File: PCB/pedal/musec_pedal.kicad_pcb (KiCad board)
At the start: 2 copper layers, 140 x 22 mm, 12 parts, among them J1 Pedal, J2 SW1, J3 SW2

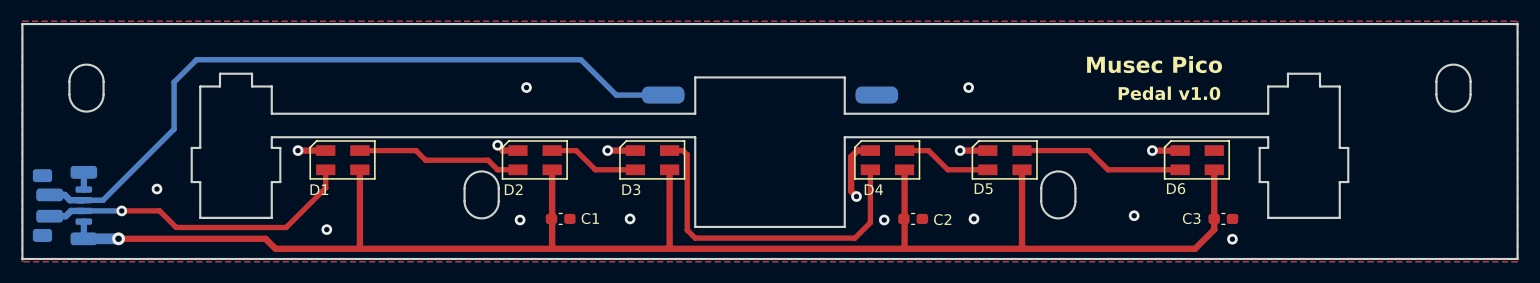
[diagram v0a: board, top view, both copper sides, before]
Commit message: Pedal PCB v1.1 (fix stabilizer position)
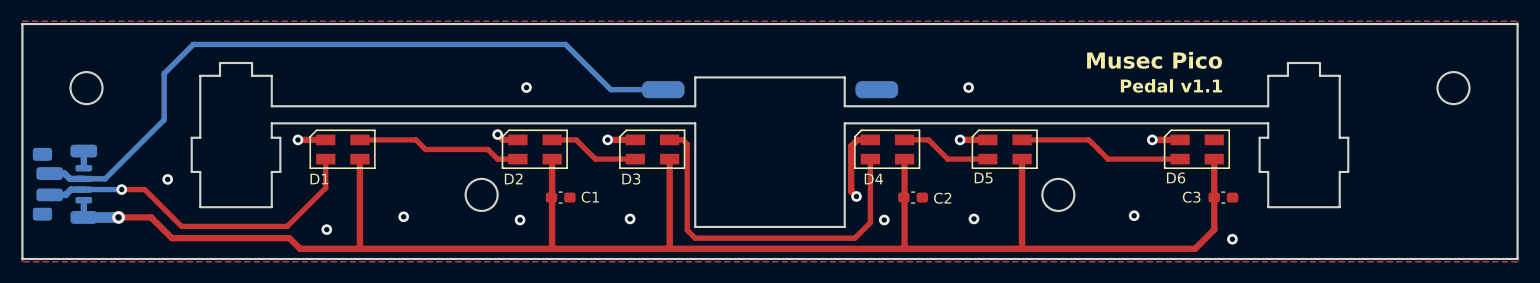
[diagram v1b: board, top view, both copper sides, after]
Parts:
- moved C1 2.00 mm to (194.6, 149.1)
- moved C2 2.00 mm to (227.6, 149.1)
- moved C3 2.00 mm to (256.6, 149.1)
- moved J1 2.00 mm to (147.9, 147.8)
- moved D1 1.00 mm to (174.2, 144.6)
- moved D2 1.00 mm to (192.2, 144.6)
- moved D3 1.00 mm to (203.2, 144.6)
- moved D4 1.00 mm to (225.2, 144.6)
- moved D5 1.00 mm to (236.2, 144.6)
- moved D6 1.00 mm to (254.2, 144.6)
- moved J2 0.50 mm to (204.2, 139.0)
- moved J3 0.50 mm to (224.2, 139.0)
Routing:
- net +5V: track 151.2 -> 158.1 mm
- net Net-(D3-Out): track 31.9 -> 33.9 mm
- net Net-(D1-In): track 29.9 -> 31.7 mm
- net GND: track 20.1 -> 21.1 mm, vias 16 -> 17
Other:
- outline, holes or cut-outs redrawn
- board text added: "Pedal v1.1"
- board text removed: "Pedal v1.0"

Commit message: Pedal PCB v1.2 (more accurate holes)
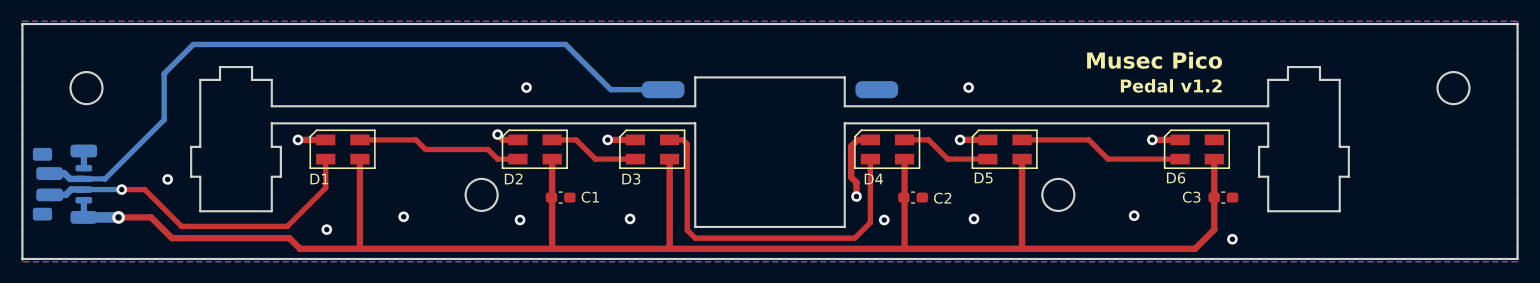
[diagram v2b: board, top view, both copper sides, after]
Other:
- outline, holes or cut-outs redrawn
- board text added: "Pedal v1.2"
- board text removed: "Pedal v1.1"

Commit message: Pedal v1.21, better SH1.0 footprint
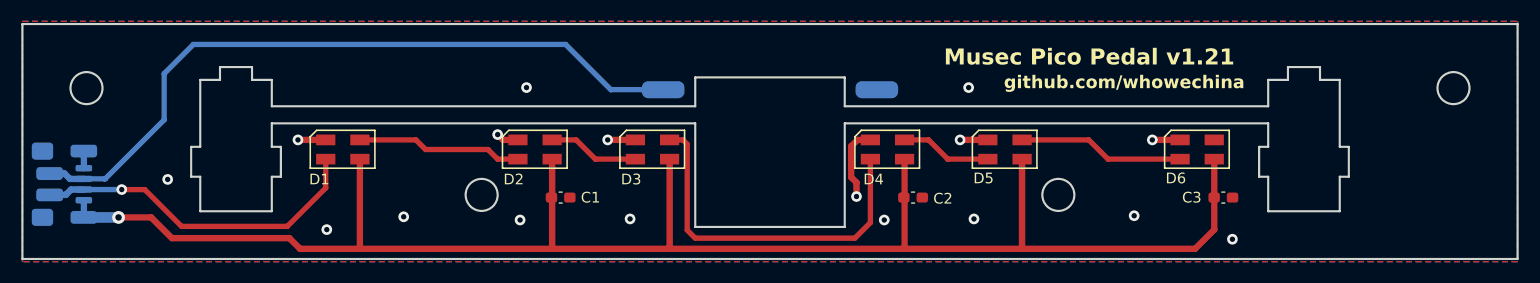
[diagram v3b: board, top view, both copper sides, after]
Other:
- board text added: "Musec Pico Pedal v1.21"
- board text added: "github.com/whowechina"
- board text removed: "Musec Pico"
- board text removed: "Pedal v1.2"

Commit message: pedal pcb v1.22, finetune
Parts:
- moved J2 0.30 mm to (204.2, 139.3)
- moved J3 0.30 mm to (224.2, 139.3)
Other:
- board text added: "Musec Pico Pedal v1.22"
- board text removed: "Musec Pico Pedal v1.21"
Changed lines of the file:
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@@
 		(layer "F.Cu")
 		(at 194.596 149.074)
-		(descr "Capacitor SMD 0603 (1608 Metric), square (rectangular) end terminal, IPC_7351 nominal with elongated pad for handsoldering. (Body size source: IPC-SM-782 page 76, https://www.pcb-3d.com/wordpress/wp-content/uploads/ipc-sm-782a_amendment_1_and_2.pdf), generated with kicad-footprint-generator")
+		(descr "Capacitor SMD 0603 (1608 Metric), square (rectangular) end terminal, IPC-7351 nominal with elongated pad for handsoldering. (Body size source: IPC-SM-782 page 76, https://www.pcb-3d.com/wordpress/wp-content/uploads/ipc-sm-782a_amendment_1_and_2.pdf), generated with kicad-footprint-generator")
 		(tags "capacitor handsolder")
 		(property "Reference" "C1"
@@
 		)
 		(embedded_fonts no)
-		(model "${KICAD8_3DMODEL_DIR}/Capacitor_SMD.3dshapes/C_0603_1608Metric.wrl"
+		(model "${KICAD9_3DMODEL_DIR}/Capacitor_SMD.3dshapes/C_0603_1608Metric.step"
 			(offset
 				(xyz 0 0 0)
@@
 		(layer "F.Cu")
 		(at 227.596 149.074)
-		(descr "Capacitor SMD 0603 (1608 Metric), square (rectangular) end terminal, IPC_7351 nominal with elongated pad for handsoldering. (Body size source: IPC-SM-782 page 76, https://www.pcb-3d.com/wordpress/wp-content/uploads/ipc-sm-782a_amendment_1_and_2.pdf), generated with kicad-footprint-generator")
+		(descr "Capacitor SMD 0603 (1608 Metric), square (rectangular) end terminal, IPC-7351 nominal with elongated pad for handsoldering. (Body size source: IPC-SM-782 page 76, https://www.pcb-3d.com/wordpress/wp-content/uploads/ipc-sm-782a_amendment_1_and_2.pdf), generated with kicad-footprint-generator")
 		(tags "capacitor handsolder")
 		(property "Reference" "C2"
@@
 		)
 		(embedded_fonts no)
-		(model "${KICAD8_3DMODEL_DIR}/Capacitor_SMD.3dshapes/C_0603_1608Metric.wrl"
+		(model "${KICAD9_3DMODEL_DIR}/Capacitor_SMD.3dshapes/C_0603_1608Metric.step"
 			(offset
 				(xyz 0 0 0)
@@
 		(layer "F.Cu")
 		(at 256.646 149.074)
-		(descr "Capacitor SMD 0603 (1608 Metric), square (rectangular) end terminal, IPC_7351 nominal with elongated pad for handsoldering. (Body size source: IPC-SM-782 page 76, https://www.pcb-3d.com/wordpress/wp-content/uploads/ipc-sm-782a_amendment_1_and_2.pdf), generated with kicad-footprint-generator")
+		(descr "Capacitor SMD 0603 (1608 Metric), square (rectangular) end terminal, IPC-7351 nominal with elongated pad for handsoldering. (Body size source: IPC-SM-782 page 76, https://www.pcb-3d.com/wordpress/wp-content/uploads/ipc-sm-782a_amendment_1_and_2.pdf), generated with kicad-footprint-generator")
 		(tags "capacitor handsolder")
 		(property "Reference" "C3"
@@
 		)
 		(embedded_fonts no)
-		(model "${KICAD8_3DMODEL_DIR}/Capacitor_SMD.3dshapes/C_0603_1608Metric.wrl"
+		(model "${KICAD9_3DMODEL_DIR}/Capacitor_SMD.3dshapes/C_0603_1608Metric.step"
 			(offset
 				(xyz 0 0 0)
@@
 	(footprint "musec_pedal:Solder_1P"
 		(layer "B.Cu")
-		(at 204.196 138.974)
+		(at 204.196 139.274)
 		(descr "Through hole straight pin header, 1x05, 2.54mm pitch, single row")
 		(tags "Through hole pin header THT 1x05 2.54mm single row")
@@
 		(attr smd)
 		(fp_rect
-			(start 2.3 -1.01)
-			(end -2.3 1.09)
+			(start -2.3 1.09)
+			(end 2.3 -1.01)
 			(stroke
 				(width 0.12)
@@
 	(footprint "musec_pedal:Solder_1P"
 		(layer "B.Cu")
-		(at 224.196 138.974 180)
+		(at 224.196 139.274 180)
 		(descr "Through hole straight pin header, 1x05, 2.54mm pitch, single row")
 		(tags "Through hole pin header THT 1x05 2.54mm single row")
@@
 		(attr smd)
 		(fp_rect
-			(start 2.3 -1.01)
-			(end -2.3 1.09)
+			(start -2.3 1.09)
+			(end 2.3 -1.01)
 			(stroke
 				(width 0.12)
@@
 		(layer "Edge.Cuts")
 	)
-	(gr_text "Musec Pico Pedal v1.21"
+	(gr_text "Musec Pico Pedal v1.22"
 		(at 230.476 136.794 0)
 		(layer "F.SilkS")
@@
 	)
 	(segment
+		(start 157.466 141.804)
+		(end 151.946 147.324)
+		(width 0.5)
+		(layer "B.Cu")
+		(net 10)
+	)
+	(segment
+		(start 199.596 139.274)
+		(end 195.056 134.734)
+		(width 0.5)
+		(layer "B.Cu")
+		(net 10)
+	)
+	(segment
 		(start 148.646 147.324)
 		(end 148.146 146.824)
@@
 	)
 	(segment
-		(start 157.466 141.804)
-		(end 151.946 147.324)
+		(start 204.196 139.274)
+		(end 199.596 139.274)
 		(width 0.5)
 		(layer "B.Cu")
@@
 	)
 	(segment
-		(start 160.206 134.734)
-		(end 157.466 137.474)
+		(start 157.466 137.474)
+		(end 157.466 141.804)
 		(width 0.5)
 		(layer "B.Cu")
@@
 	)
 	(segment
-		(start 157.466 137.474)
-		(end 157.466 141.804)
+		(start 160.206 134.734)
+		(end 157.466 137.474)
 		(width 0.5)
 		(layer "B.Cu")
@@
 	)
 	(segment
-		(start 199.296 138.974)
-		(end 195.056 134.734)
-		(width 0.5)
-		(layer "B.Cu")
-		(net 10)
-	)
-	(segment
 		(start 149.946 147.324)
 		(end 148.646 147.324)
@@
 		(layer "B.Cu")
 		(net 10)
-	)
-	(segment
-		(start 204.196 138.974)
-		(end 199.296 138.974)
-		(width 0.5)
-		(layer "B.Cu")
-		(net 10)
